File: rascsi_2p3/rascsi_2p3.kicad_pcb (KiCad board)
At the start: 2 copper layers, 65 x 56 mm, 105 parts, among them IC1 SN74LS641-1DW, IC2 SN74LS641-1DW, IC3 SN74LS641-1DW, IC4 SN74LS641-1DW, J1 Raspberry_Pi_2_3, J2 Conn_01x02_Male, J3 Conn_02x25_Odd_Even, J4 I2C Pinout, J5 Conn_02x03_Odd_Even, J6 CONNFLY DB-25, J7 Conn_01x02_Male, J8 USB_B_Micro, U1 24LC256, X1 Mac, X2 Dogcow, X3 Mac, X4 Dogcow, X5 Dogcow, X6 Dogcow, X7 Pi, X8 Pi

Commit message: Commit ordered version of the board
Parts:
- removed JP1, JP2, JP3, JP4: Jumper_3_Bridged12, Jumper:SolderJumper-3_P1.3mm_Bridged2Bar12_Pad1.0x1.5mm
- removed R59, R60, R61, R62: 10k, Resistor_SMD:R_0402_1005Metric
- removed R63, R64: 4.7k, Resistor_SMD:R_0402_1005Metric
- removed U1: 24LC256, Package_SO:SOIC-8-1EP_3.9x4.9mm_P1.27mm_EP2.41x3.3mm
- moved R22 2.54 mm to (194.3, 50.6)
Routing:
- net PI_SDA: track 61.8 -> 13.2 mm, vias 2 -> 0
- net PI_SCL: track 67.1 -> 20.2 mm, vias 3 -> 1
- net +3V3: track 130.4 -> 95.2 mm, vias 10 -> 4
- net Net-(JP3-Pad2): track 13.4 -> 0.00 mm, vias 1 -> 0
- net Net-(JP2-Pad2): track 12.4 -> 0.00 mm, vias 1 -> 0
- net Net-(JP4-Pad2): track 9.15 -> 0.00 mm, vias 1 -> 0
- net DBG_LED: track 23.8 -> 16.4 mm, vias 1 -> 0
- net /TERM_GND: track 74.7 -> 69.3 mm
- net GND: track 385.5 -> 390.5 mm, vias 90 -> 82
- net PI-BSY: track 27.7 -> 32.5 mm
- net /TERM_5v: track 72.2 -> 68.0 mm
- net Net-(JP1-Pad2): track 3.32 -> 0.00 mm, vias 1 -> 0
- net PI-ACT: track 57.0 -> 54.2 mm
- net PI-D7: track 17.1 -> 14.9 mm
- net PI-DP: track 9.86 -> 11.9 mm
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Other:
- board text removed: "A0"
- board text removed: "A1"
- board text removed: "A2"
- board text removed: "EEPROM"
- board text removed: "Read"
- board text removed: "Write"

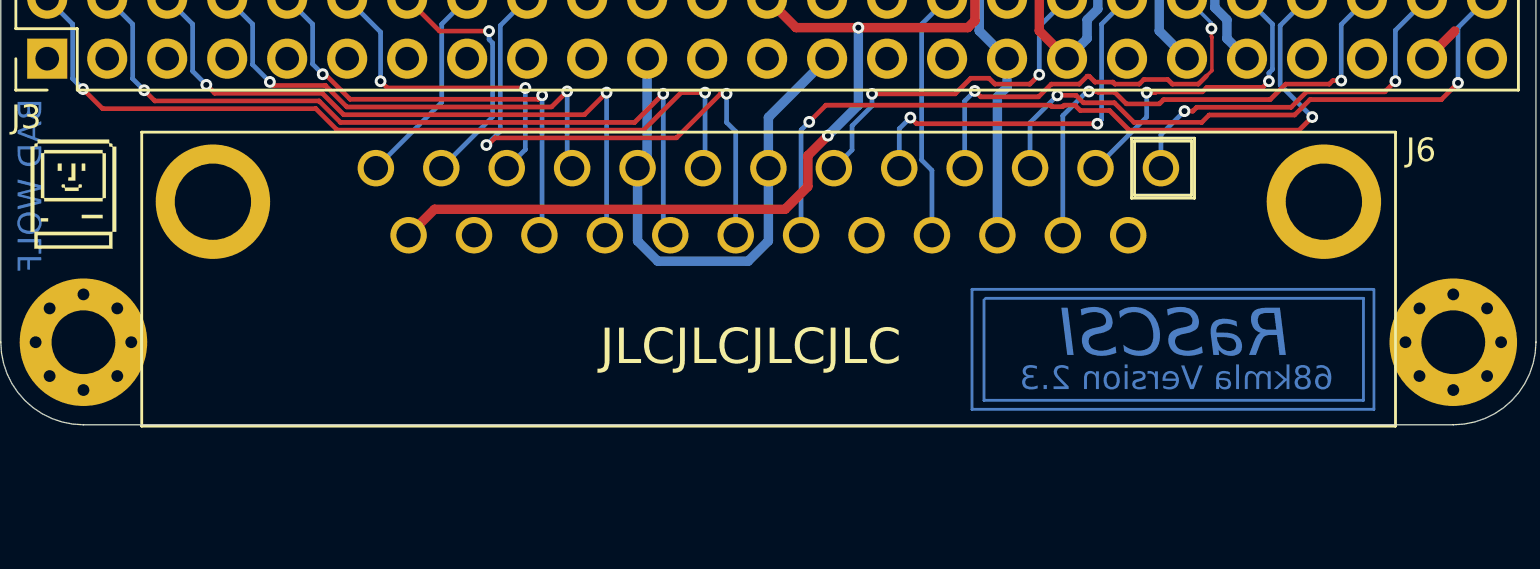
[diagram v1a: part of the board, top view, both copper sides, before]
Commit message: Added STEP file and updated symbol and 3d model references to reference the correct gender of parts. Should be no functional change
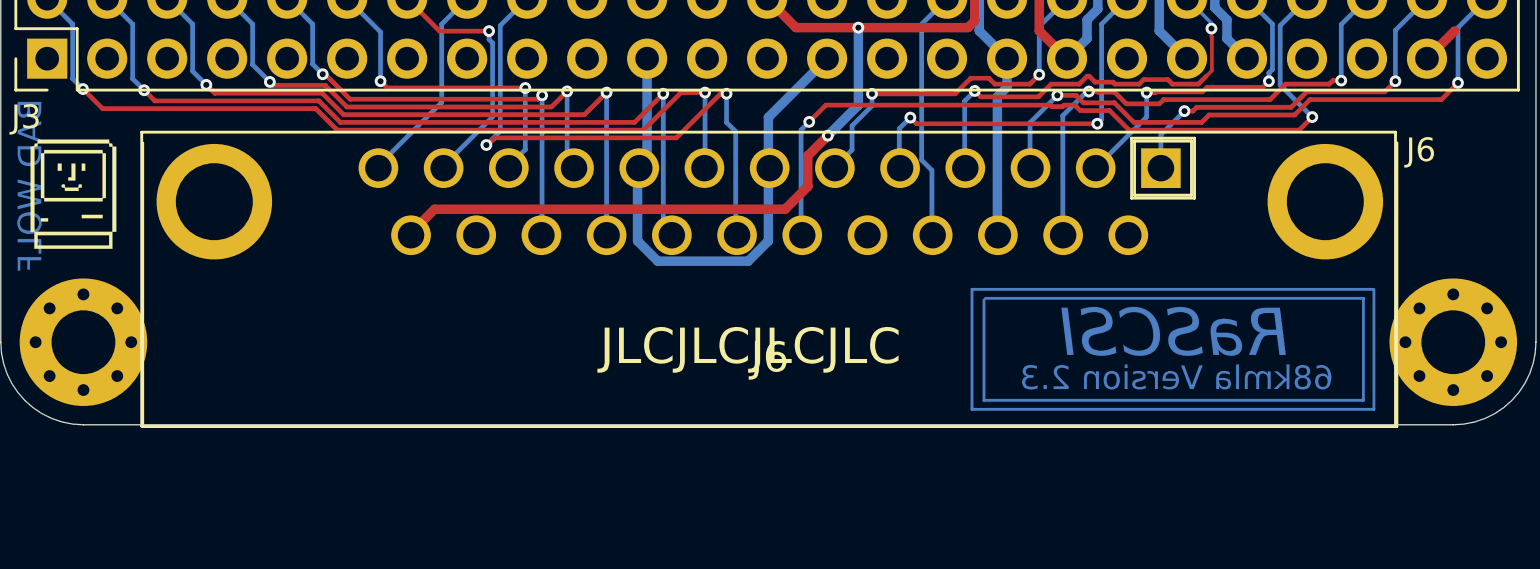
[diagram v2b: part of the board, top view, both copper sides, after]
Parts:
- J2, J7: value Conn_01x02_Male -> DNP
- J5: value Conn_02x03_Odd_Even -> DNP
- J6: footprint SamacSys_Parts:L717SDB25PA4CH4F -> SamacSys_Parts:57489011; moved to F.Cu
- R3: value 5k -> 5.1k
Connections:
- J3 pad 25: Net-(J3-Pad25) -> (no net)
- J3 pad 34: Net-(J3-Pad34) -> (no net)
